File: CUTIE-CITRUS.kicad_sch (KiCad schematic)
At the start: 0 parts

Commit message: added misc
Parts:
- added D?: LED Green, LED_SMD:LED_0603_1608Metric, symbol Device:LED
- added J?: Conn_01x03, Connector_PinHeader_2.54mm:PinHeader_1x03_P2.54mm_Vertical, symbol Connector_Generic:Conn_01x03
- added R?: 1k, Resistor_SMD:R_0402_1005Metric, symbol Device:R
- added TP?: TestPoint, TestPoint:TestPoint_Pad_2.0x2.0mm, symbol Connector:TestPoint
- added U1: CM5, CM5IO:Raspberry-Pi-5-Compute-Module, symbol CM5IO:ComputeModule5-CM5
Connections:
- new net: D?.1 (K), R?.1, TP?.1
- new net: R?.2, U1.21 (LED_nACT)
- new net +1.8v: U1.88 (+1.8v_(Output)), U1.90 (+1.8v_(Output))
- new net +3.3v: D?.2 (A), U1.84 (+3.3v_(Output)), U1.86 (+3.3v_(Output))
- new net +5v: U1.77 (+5v_(Input)), U1.79 (+5v_(Input)), U1.81 (+5v_(Input)), U1.83 (+5v_(Input)), U1.85 (+5v_(Input)), U1.87 (+5v_(Input))
- new net BT_nDis: J?.3 (Pin_3), U1.91 (BT_nDisable)
- new net CAM_GPIO0: U1.97 (CAM_GPIO0)
- new net CAM_GPIO1: U1.100 (CAM_GPIO1)
- new net CC1: U1.94 (CC1)
- new net CC2: U1.96 (CC2)
- new net DPHY0_C_N: U1.127 (MIPI0_C_N)
- new net DPHY0_C_P: U1.129 (MIPI0_C_P)
- new net DPHY0_D0_N: U1.115 (MIPI0_D0_N)
- new net DPHY0_D0_P: U1.117 (MIPI0_D0_P)
- new net DPHY0_D1_N: U1.121 (MIPI0_D1_N)
- new net DPHY0_D1_P: U1.123 (MIPI0_D1_P)
- new net DPHY0_D2_N: U1.133 (MIPI0_D2_N)
- new net DPHY0_D2_P: U1.135 (MIPI0_D2_P)
- new net DPHY0_D3_N: U1.139 (MIPI0_D3_N)
- new net DPHY0_D3_P: U1.141 (MIPI0_D3_P)
- new net DPHY1_C_N: U1.187 (MIPI1_C_N)
- new net DPHY1_C_P: U1.189 (MIPI1_C_P)
- new net DPHY1_D0_N: U1.175 (MIPI1_D0_N)
- new net DPHY1_D0_P: U1.177 (MIPI1_D0_P)
- new net DPHY1_D1_N: U1.181 (MIPI1_D1_N)
- new net DPHY1_D1_P: U1.183 (MIPI1_D1_P)
- new net DPHY1_D2_N: U1.193 (MIPI1_D2_N)
- new net DPHY1_D2_P: U1.195 (MIPI1_D2_P)
- new net DPHY1_D3_N: U1.194 (MIPI1_D3_N)
- new net DPHY1_D3_P: U1.196 (MIPI1_D3_P)
- new net EEPROM_nWP: U1.20 (EEPROM_nWP)
- new net ETH_LEDG: U1.17 (Ethernet_nLED2(3.3v))
- new net ETH_LEDY: U1.15 (Ethernet_nLED3(3.3v))
- new net GND: J?.2 (Pin_2), U1.1 (GND), U1.107 (GND), U1.108 (GND), U1.113 (GND), U1.114 (GND), U1.119 (GND), U1.120 (GND), U1.125 (GND), U1.126 (GND), U1.13 (GND), U1.131 (GND), U1.132 (GND), U1.137 (GND), U1.138 (GND), U1.14 (GND), U1.144 (GND), U1.150 (GND), U1.155 (GND), U1.156 (GND), U1.161 (GND), U1.162 (GND), U1.167 (GND), U1.168 (GND), U1.173 (GND), U1.174 (GND), U1.179 (GND), U1.180 (GND), U1.185 (GND), U1.186 (GND), U1.191 (GND), U1.192 (GND), U1.197 (GND), U1.198 (GND), U1.2 (GND), U1.22 (GND), U1.23 (GND), U1.32 (GND), U1.33 (GND), U1.42 (GND), U1.43 (GND), U1.52 (GND), U1.53 (GND), U1.59 (GND), U1.60 (GND), U1.65 (GND), U1.66 (GND), U1.7 (GND), U1.71 (GND), U1.74 (GND), U1.8 (GND), U1.98 (GND)
- new net GPIO10: U1.44 (GPIO10)
- new net GPIO11: U1.38 (GPIO11)
- new net GPIO12: U1.31 (GPIO12)
- new net GPIO13: U1.28 (GPIO13)
- new net GPIO14: U1.55 (GPIO14)
- new net GPIO15: U1.51 (GPIO15)
- new net GPIO16: U1.29 (GPIO16)
- new net GPIO17: U1.50 (GPIO17)
- new net GPIO18: U1.49 (GPIO18)
- new net GPIO19: U1.26 (GPIO19)
- new net GPIO2: U1.58 (GPIO2)
- new net GPIO20: U1.27 (GPIO20)
- new net GPIO21: U1.25 (GPIO21)
- new net GPIO22: U1.46 (GPIO22)
- new net GPIO23: U1.47 (GPIO23)
- new net GPIO24: U1.45 (GPIO24)
- new net GPIO25: U1.41 (GPIO25)
- new net GPIO26: U1.24 (GPIO26)
- new net GPIO27: U1.48 (GPIO27)
- new net GPIO3: U1.56 (GPIO3)
- new net GPIO4: U1.54 (GPIO4)
- new net GPIO5: U1.34 (GPIO5)
- new net GPIO6: U1.30 (GPIO6)
- new net GPIO7: U1.37 (GPIO7)
- new net GPIO8: U1.39 (GPIO8)
- new net GPIO9: U1.40 (GPIO9)
- new net GPIO_VREF: U1.78 (GPIO_VREF(1.8v/3.3v_Input))
- new net HDMI0_CEC: U1.151 (HDMI0_CEC)
- new net HDMI0_CK_N: U1.190 (HDMI0_CLK_N)
- new net HDMI0_CK_P: U1.188 (HDMI0_CLK_P)
- new net HDMI0_D0_N: U1.184 (HDMI0_TX0_N)
- new net HDMI0_D0_P: U1.182 (HDMI0_TX0_P)
- new net HDMI0_D1_N: U1.178 (HDMI0_TX1_N)
- new net HDMI0_D1_P: U1.176 (HDMI0_TX1_P)
- new net HDMI0_D2_N: U1.172 (HDMI0_TX2_N)
- new net HDMI0_D2_P: U1.170 (HDMI0_TX2_P)
- new net HDMI0_HOTPLUG: U1.153 (HDMI0_HOTPLUG)
- new net HDMI0_SCL: U1.200 (HDMI0_SCL)
- new net HDMI0_SDA: U1.199 (HDMI0_SDA)
- new net HDMI1_CEC: U1.149 (HDMI1_CEC)
- new net HDMI1_CK_N: U1.166 (HDMI1_CLK_N)
- new net HDMI1_CK_P: U1.164 (HDMI1_CLK_P)
- new net HDMI1_D0_N: U1.160 (HDMI1_TX0_N)
- new net HDMI1_D0_P: U1.158 (HDMI1_TX0_P)
- new net HDMI1_D1_N: U1.154 (HDMI1_TX1_N)
- new net HDMI1_D1_P: U1.152 (HDMI1_TX1_P)
- new net HDMI1_D2_N: U1.148 (HDMI1_TX2_N)
- new net HDMI1_D2_P: U1.146 (HDMI1_TX2_P)
- new net HDMI1_HOTPLUG: U1.143 (HDMI1_HOTPLUG)
- new net HDMI1_SCL: U1.147 (HDMI1_SCL)
- new net HDMI1_SDA: U1.145 (HDMI1_SDA)
- new net ID_SC: U1.35 (ID_SC)
- new net ID_SD: U1.36 (ID_SD)
- new net PCIE_CLK_N: U1.112 (PCIe_CLK_N)
- new net PCIE_CLK_P: U1.110 (PCIe_CLK_P)
- new net PCIE_PWR_EN: U1.106 (PCIE_PWR_EN)
- new net PCIE_RX_N: U1.118 (PCIe_RX_N)
- new net PCIE_RX_P: U1.116 (PCIe_RX_P)
- new net PCIE_TX_N: U1.124 (PCIe_TX_N)
- new net PCIE_TX_P: U1.122 (PCIe_TX_P)
- new net PCIE_nCLKREQ: U1.102 (PCIe_nCLKREQ)
- new net PCIE_nRST: U1.109 (PCIe_nRST)
- new net PCIE_nWAKE: U1.104 (PCIE_nWAKE)
- new net PMIC_ENABLE: U1.99 (PMIC_ENABLE)
- new net PWM: U1.19 (FAN_PWM)
- new net PWR_BUT: U1.92 (PWR_BUT)
- new net SCL0: U1.80 (SCL0)
- new net SDA0: U1.82 (SDA0)
- new net SD_CLK: U1.57 (SD_CLK)
- new net SD_CMD: U1.62 (SD_CMD)
- new net SD_DAT0: U1.63 (SD_DAT0)
- new net SD_DAT1: U1.67 (SD_DAT1)
- new net SD_DAT2: U1.69 (SD_DAT2)
- new net SD_DAT3: U1.61 (SD_DAT3)
- new net SD_PWR_ON: U1.75 (SD_PWR_ON)
- new net SYNC_OUT: U1.18 (Ethernet_SYNC_OUT(3.3v))
- new net TACHO: U1.16 (FAN_TACHO)
- new net TRD0_N: U1.10 (Ethernet_Pair0_N)
- new net TRD0_P: U1.12 (Ethernet_Pair0_P)
- new net TRD1_N: U1.6 (Ethernet_Pair1_N)
- new net TRD1_P: U1.4 (Ethernet_Pair1_P)
- new net TRD2_N: U1.9 (Ethernet_Pair2_N)
- new net TRD2_P: U1.11 (Ethernet_Pair2_P)
- new net TRD3_N: U1.5 (Ethernet_Pair3_N)
- new net TRD3_P: U1.3 (Ethernet_Pair3_P)
- new net USB2_N: U1.103 (USB2_N)
- new net USB2_P: U1.105 (USB2_P)
- new net USB3-0-D_N: U1.136 (USB3-0-D_N)
- new net USB3-0-D_P: U1.134 (USB3-0-D_P)
- new net USB3-0-RX_N: U1.128 (USB3-0-RX_N)
- new net USB3-0-RX_P: U1.130 (USB3-0-RX_P)
- new net USB3-0-TX_N: U1.140 (USB3-0-TX_N)
- new net USB3-0-TX_P: U1.142 (USB3-0-TX_P)
- new net USB3-1-D_N: U1.165 (USB3-1-D_N)
- new net USB3-1-D_P: U1.163 (USB3-1-D_P)
- new net USB3-1-RX_N: U1.157 (USB3-1-RX_N)
- new net USB3-1-RX_P: U1.159 (USB3-1-RX_P)
- new net USB3-1-TX_N: U1.169 (USB3-1-TX_N)
- new net USB3-1-TX_P: U1.171 (USB3-1-TX_P)
- new net USBOTG_ID: U1.101 (USB_OTG_ID)
- new net VBAT: U1.76 (VBAT)
- new net VBUS_EN: U1.111 (VBUS_EN)
- new net WL_nDis: J?.1 (Pin_1), U1.89 (WiFi_nDisable)
- new net nPWR_LED: U1.95 (LED_nPWR)
- new net nRPIBOOT: U1.93 (nRPIBOOT)
- no-connect marks 0 -> 5
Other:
- note added: "Activity LED"
- note added: "Not Fitted header"

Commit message: saved libs to project, initialized hierarchy
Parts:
- removed D?: LED Green, LED_SMD:LED_0603_1608Metric, symbol Device:LED
- removed J?: Conn_01x03, Connector_PinHeader_2.54mm:PinHeader_1x03_P2.54mm_Vertical, symbol Connector_Generic:Conn_01x03
- removed R?: 1k, Resistor_SMD:R_0402_1005Metric, symbol Device:R
- removed TP?: TestPoint, TestPoint:TestPoint_Pad_2.0x2.0mm, symbol Connector:TestPoint
- removed U1: CM5, CM5IO:Raspberry-Pi-5-Compute-Module, symbol CM5IO:ComputeModule5-CM5
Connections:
- no-connect marks 5 -> 0
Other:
- added sheet CM5 Connectors (cm5.kicad_sch)
- note removed: "Activity LED"
- note removed: "Not Fitted header"

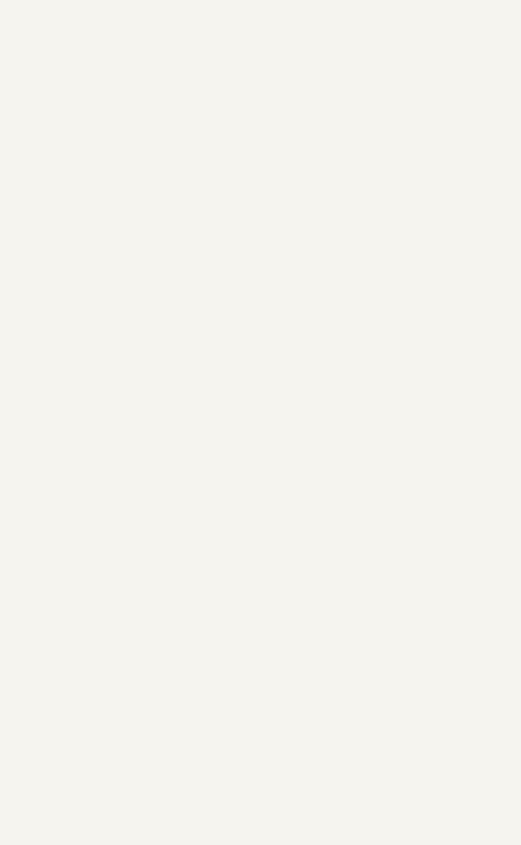
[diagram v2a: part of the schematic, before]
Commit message: added fpc connector
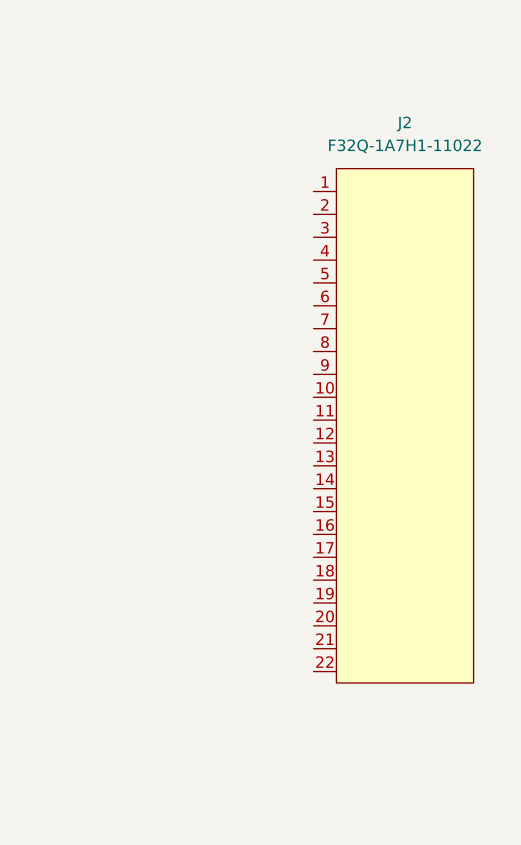
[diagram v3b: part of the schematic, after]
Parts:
- added J2: F32Q-1A7H1-11022, symbol library:F32Q-1A7H1-11022
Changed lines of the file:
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@@
 	(generator_version "9.0")
 	(paper "A4")
+	(symbol
+		(lib_id "library:F32Q-1A7H1-11022")
+		(at 220.98 91.44 0)
+		(unit 1)
+		(exclude_from_sim no)
+		(in_bom yes)
+		(on_board yes)
+		(dnp no)
+		(property "Reference" "J2"
+			(at 220.98 58.42 0)
+			(effects
+				(font
+					(size 1.27 1.27)
+				)
+			)
+		)
+		(property "Value" "F32Q-1A7H1-11022"
+			(at 220.98 60.96 0)
+			(effects
+				(font
+					(size 1.27 1.27)
+				)
+			)
+		)
+		(property "Footprint" ""
+			(at 220.98 91.44 0)
+			(effects
+				(font
+					(size 1.27 1.27)
+				)
+				(hide yes)
+			)
+		)
+		(property "Datasheet" "https://cdn.amphenol-cs.com/media/wysiwyg/files/documentation/datasheet/flex/ffc_fpc_050mm_f32r_f32q.pdf"
+			(at 220.98 77.47 0)
+			(effects
+				(font
+					(size 1.27 1.27)
+				)
+				(hide yes)
+			)
+		)
+		(property "Description" "22 Position FFC, FPC Connector Contacts, Top 0.020\" (0.50mm) Surface Mount, Right Angle"
+			(at 220.98 77.47 0)
+			(effects
+				(font
+					(size 1.27 1.27)
+				)
+				(hide yes)
+			)
+		)
+		(pin "15"
+		)
+		(pin "16"
+		)
+		(pin "17"
+		)
+		(pin "18"
+		)
+		(pin "19"
+		)
+		(pin "2"
+		)
+		(pin "22"
+		)
+		(pin "1"
+		)
+		(pin "14"
+		)
+		(pin "13"
+		)
+		(pin "12"
+		)
+		(pin "21"
+		)
+		(pin "20"
+		)
+		(pin "11"
+		)
+		(pin "10"
+		)
+		(pin "9"
+		)
+		(pin "8"
+		)
+		(pin "7"
+		)
+		(pin "6"
+		)
+		(pin "5"
+		)
+		(pin "4"
+		)
+		(pin "3"
+		)
+		(instances
+			(project ""
+				(path "/40af415e-5e3a-41a5-ab07-08c2181863e4"
+					(reference "J2")
+					(unit 1)
+				)
+			)
+		)
+	)
 	(sheet
 		(at 113.03 49.53)
